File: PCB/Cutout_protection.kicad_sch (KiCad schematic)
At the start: 9 parts, among them K1 G5NB, Q2 MMBT3904, U6 LM358DR2G

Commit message: pcb revive
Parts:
- TP4: value TestPoint -> CutP
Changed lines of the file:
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@@
   (symbol (lib_id "Connector:TestPoint") (at 169.545 101.6 180) (unit 1)
     (in_bom yes) (on_board yes) (fields_autoplaced)
-    (property "Reference" "TP4" (id 0) (at 170.942 104.0673 0)
+    (property "Reference" "TP4" (id 0) (at 171.45 103.6319 0)
       (effects (font (size 1.27 1.27)) (justify right))
     )
-    (property "Value" "TestPoint" (id 1) (at 170.942 106.6042 0)
+    (property "Value" "CutP" (id 1) (at 171.45 106.1719 0)
       (effects (font (size 1.27 1.27)) (justify right))
     )
@@
   (symbol (lib_id "power:PWR_FLAG") (at 66.675 43.18 0) (unit 1)
     (in_bom yes) (on_board yes) (fields_autoplaced)
-    (property "Reference" "#FLG04" (id 0) (at 66.675 41.275 0)
+    (property "Reference" "#FLG03" (id 0) (at 66.675 41.275 0)
       (effects (font (size 1.27 1.27)) hide)
     )

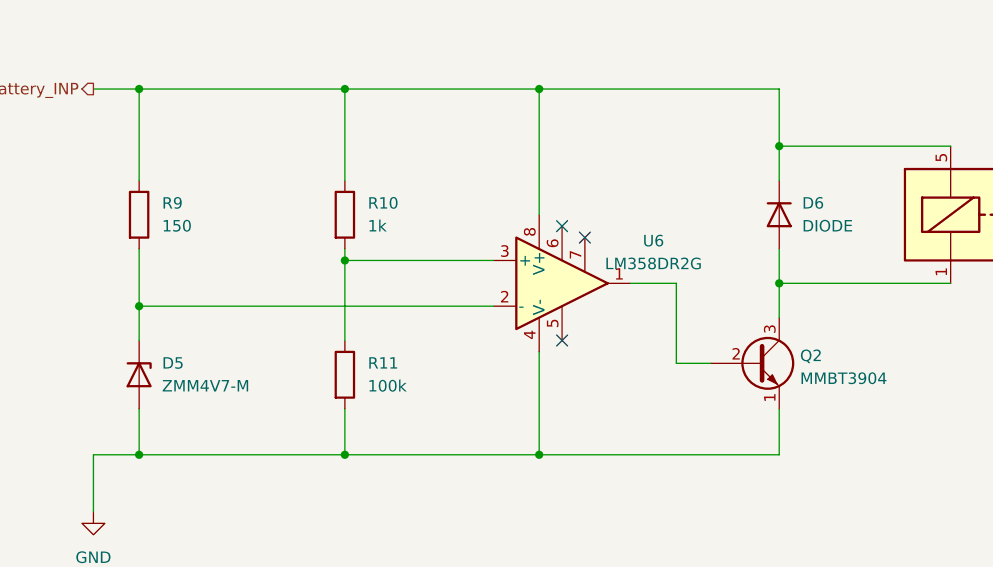
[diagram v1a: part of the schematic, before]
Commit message: Mostly addressed issues with Sensing subsystem
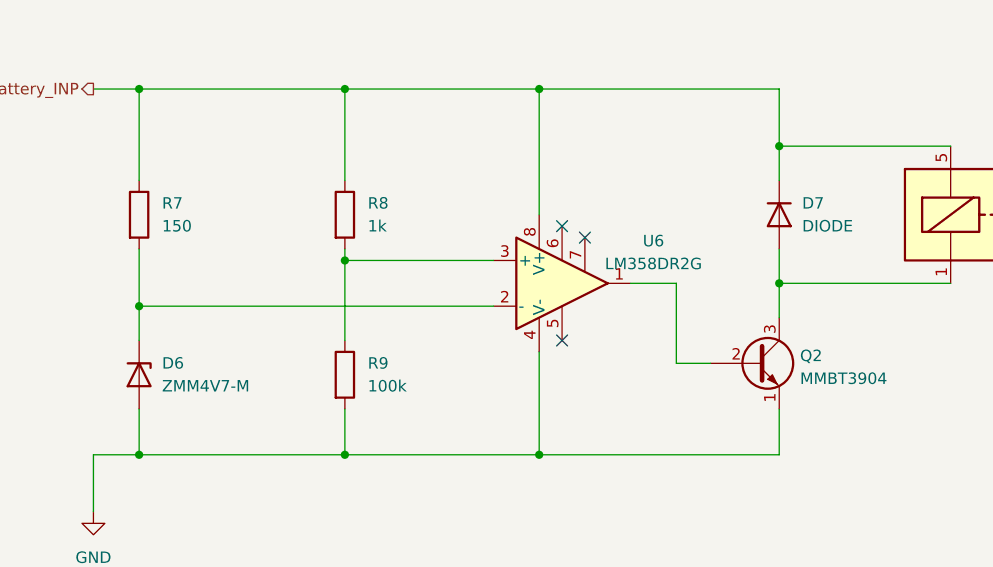
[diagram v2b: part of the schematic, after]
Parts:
- renumbered D5 to D6, D6 to D7, R9 to R7, R10 to R8, R11 to R9
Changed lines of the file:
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@@
   (symbol (lib_id "Simulation_SPICE:DIODE") (at 130.81 93.98 90) (unit 1)
     (in_bom yes) (on_board yes) (fields_autoplaced)
-    (property "Reference" "D6" (id 0) (at 133.35 92.7099 90)
+    (property "Reference" "D7" (id 0) (at 133.35 92.7099 90)
       (effects (font (size 1.27 1.27)) (justify right))
     )
@@
   (symbol (lib_id "Device:R") (at 59.69 93.98 0) (unit 1)
     (in_bom yes) (on_board yes) (fields_autoplaced)
-    (property "Reference" "R9" (id 0) (at 62.23 92.7099 0)
+    (property "Reference" "R7" (id 0) (at 62.23 92.7099 0)
       (effects (font (size 1.27 1.27)) (justify left))
     )
@@
   (symbol (lib_id "power:GND") (at 54.61 127 0) (unit 1)
     (in_bom yes) (on_board yes) (fields_autoplaced)
-    (property "Reference" "#PWR034" (id 0) (at 54.61 133.35 0)
+    (property "Reference" "#PWR033" (id 0) (at 54.61 133.35 0)
       (effects (font (size 1.27 1.27)) hide)
     )
@@
   (symbol (lib_id "Device:R") (at 82.55 93.98 0) (unit 1)
     (in_bom yes) (on_board yes) (fields_autoplaced)
-    (property "Reference" "R10" (id 0) (at 85.09 92.7099 0)
+    (property "Reference" "R8" (id 0) (at 85.09 92.7099 0)
       (effects (font (size 1.27 1.27)) (justify left))
     )
@@
   (symbol (lib_id "Device:R") (at 82.55 111.76 0) (unit 1)
     (in_bom yes) (on_board yes) (fields_autoplaced)
-    (property "Reference" "R11" (id 0) (at 85.09 110.4899 0)
+    (property "Reference" "R9" (id 0) (at 85.09 110.4899 0)
       (effects (font (size 1.27 1.27)) (justify left))
     )
@@
   (symbol (lib_id "Device:D_Zener") (at 59.69 111.76 270) (unit 1)
     (in_bom yes) (on_board yes) (fields_autoplaced)
-    (property "Reference" "D5" (id 0) (at 62.23 110.4899 90)
-      (effects (font (size 1.27 1.27)) (justify left))
-    )
+    (property "Reference" "D6" (id 0) (at 62.23 110.4899 90)
+      (effects (font (size 1.27 1.27)) (justify left))
+    )
